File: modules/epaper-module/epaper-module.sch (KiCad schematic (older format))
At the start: 24 parts, among them J1 Conn_01x04, J2 Conn_01x04, Q1 Si1308EDL, U1 WSH-12561

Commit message: EPaper module: add voltage regulator and level switch
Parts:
- added C1: 10uF, Capacitor_SMD:C_0805_2012Metric_Pad1.18x1.45mm_HandSolder, symbol Device:C
- added C13, C14: 100nF, Capacitor_SMD:C_0805_2012Metric_Pad1.18x1.45mm_HandSolder, symbol Device:C
- added C8: 4.7uF, Capacitor_SMD:C_0805_2012Metric_Pad1.18x1.45mm_HandSolder, symbol Device:C
- added U2: MIC5504-3.3YM5, Package_TO_SOT_SMD:SOT-23-5, symbol Regulator_Linear:MIC5504-3.3YM5
- added U3: TXS0108EPW, Package_SO:TSSOP-20_4.4x6.5mm_P0.65mm, symbol Logic_LevelTranslator:TXS0108EPW
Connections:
- net labels added: BUSY', CLK', CS', DC', DIN', RES', VCC
- wire segments 97 -> 135

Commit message: EPaper module: split display into display itself and connector
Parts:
- added DS1: WSH-12561, project_components:WSH-12561, symbol project_components:WSH-12561
- added JP1: Jumper_NC_Dual, Jumper:SolderJumper-3_P2.0mm_Open_TrianglePad1.0x1.5mm, symbol Device:Jumper_NC_Dual
- D1, D2, D3: VendorLink (none) -> https://pl.mouser.com/ProductDetail/onsemi/MBR0530T3G?qs=3J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
- H1, H2, H3, H4: VendorLink (none) -> N/A
- L1: value 10H -> 10uH; footprint Inductor_SMD:L_0805_2012Metric_Pad1.15x1.40mm_HandSolder -> Inductor_SMD:L_TDK_NLV25_2.5x2.0mm; VendorLink (none) -> https://pl.mouser.com/ProductDetail/739-TYA252012100M-10
- Q1: VendorLink (none) -> https://pl.mouser.com/ProductDetail/78-SI1308EDL-T1-BE3
- U2: VendorLink (none) -> https://pl.mouser.com/ProductDetail/Microchip-Technology-Mi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
- U3: VendorLink (none) -> https://pl.mouser.com/ProductDetail/771-NTS0308EPWJ
- XDS1: renamed from U1; value WSH-12561 -> WSH-12561-FFC-MP; footprint epaper-module:WSH-12561 -> Connector_FFC-FPC:TE_2-1734839-4_1x24-1MP_P0.5mm_Horizontal; symbol project_components:WSH-12561 -> project_components:WSH-12561-FFC-MP
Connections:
- net labels added: BS
- wire segments 135 -> 136
- no-connect marks 3 -> 7
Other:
- moved on the sheet: C1, C13, C14, C8, U2, U3

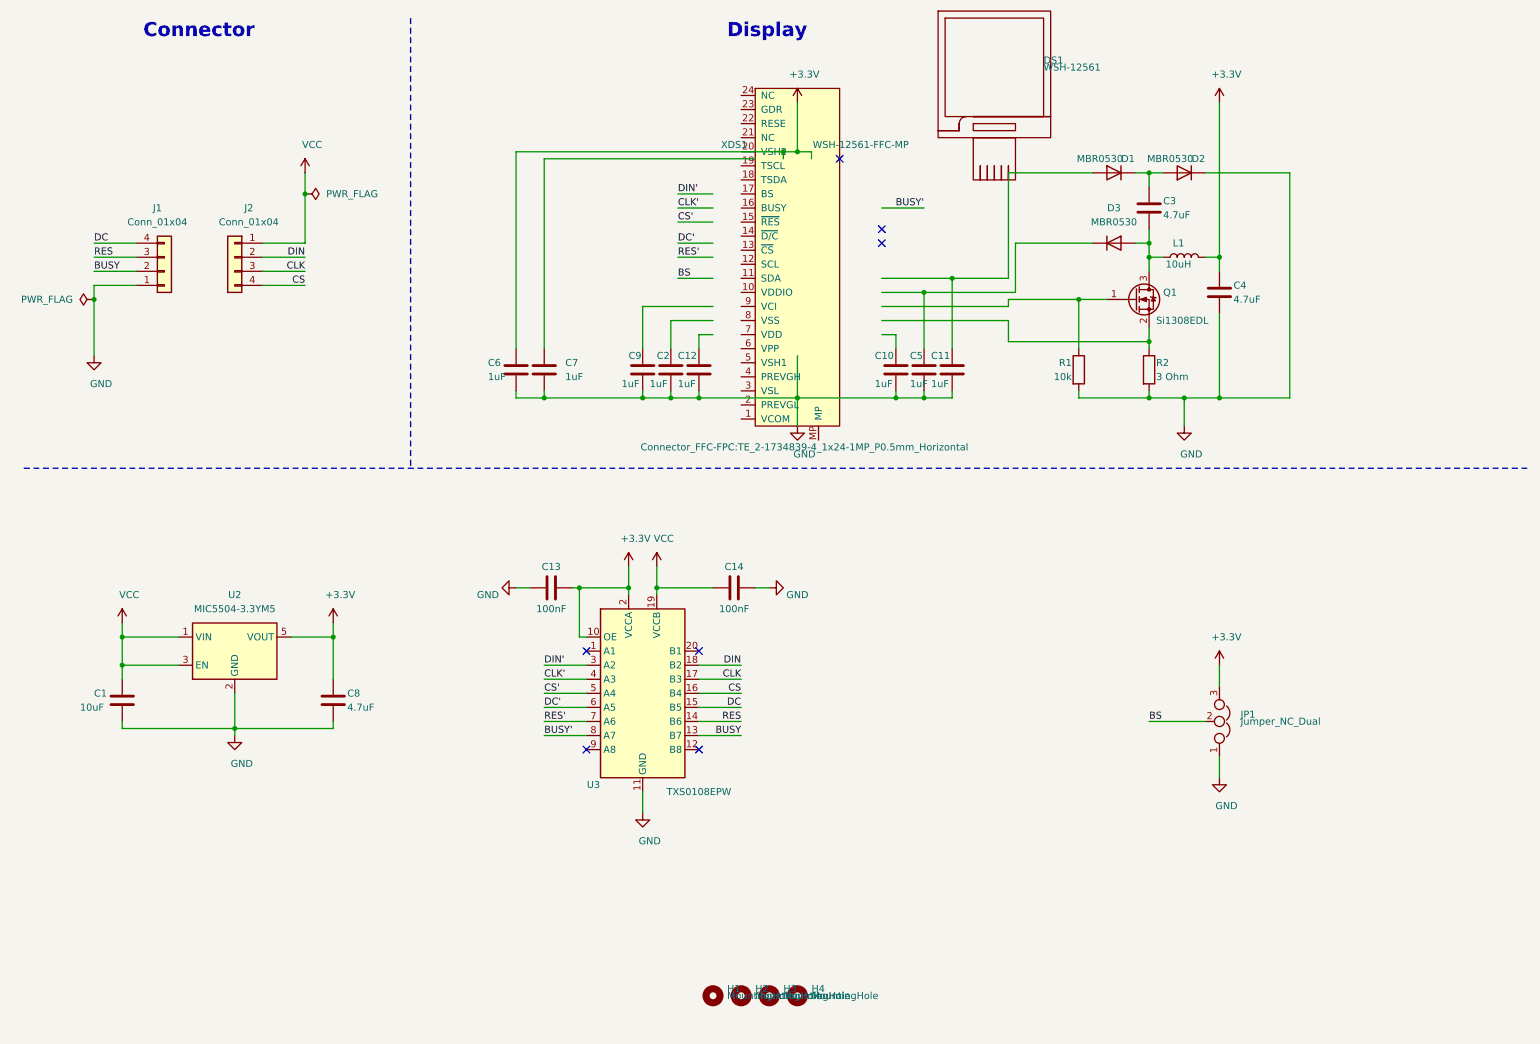
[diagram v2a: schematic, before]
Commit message: EPaper module: reorganize schematic
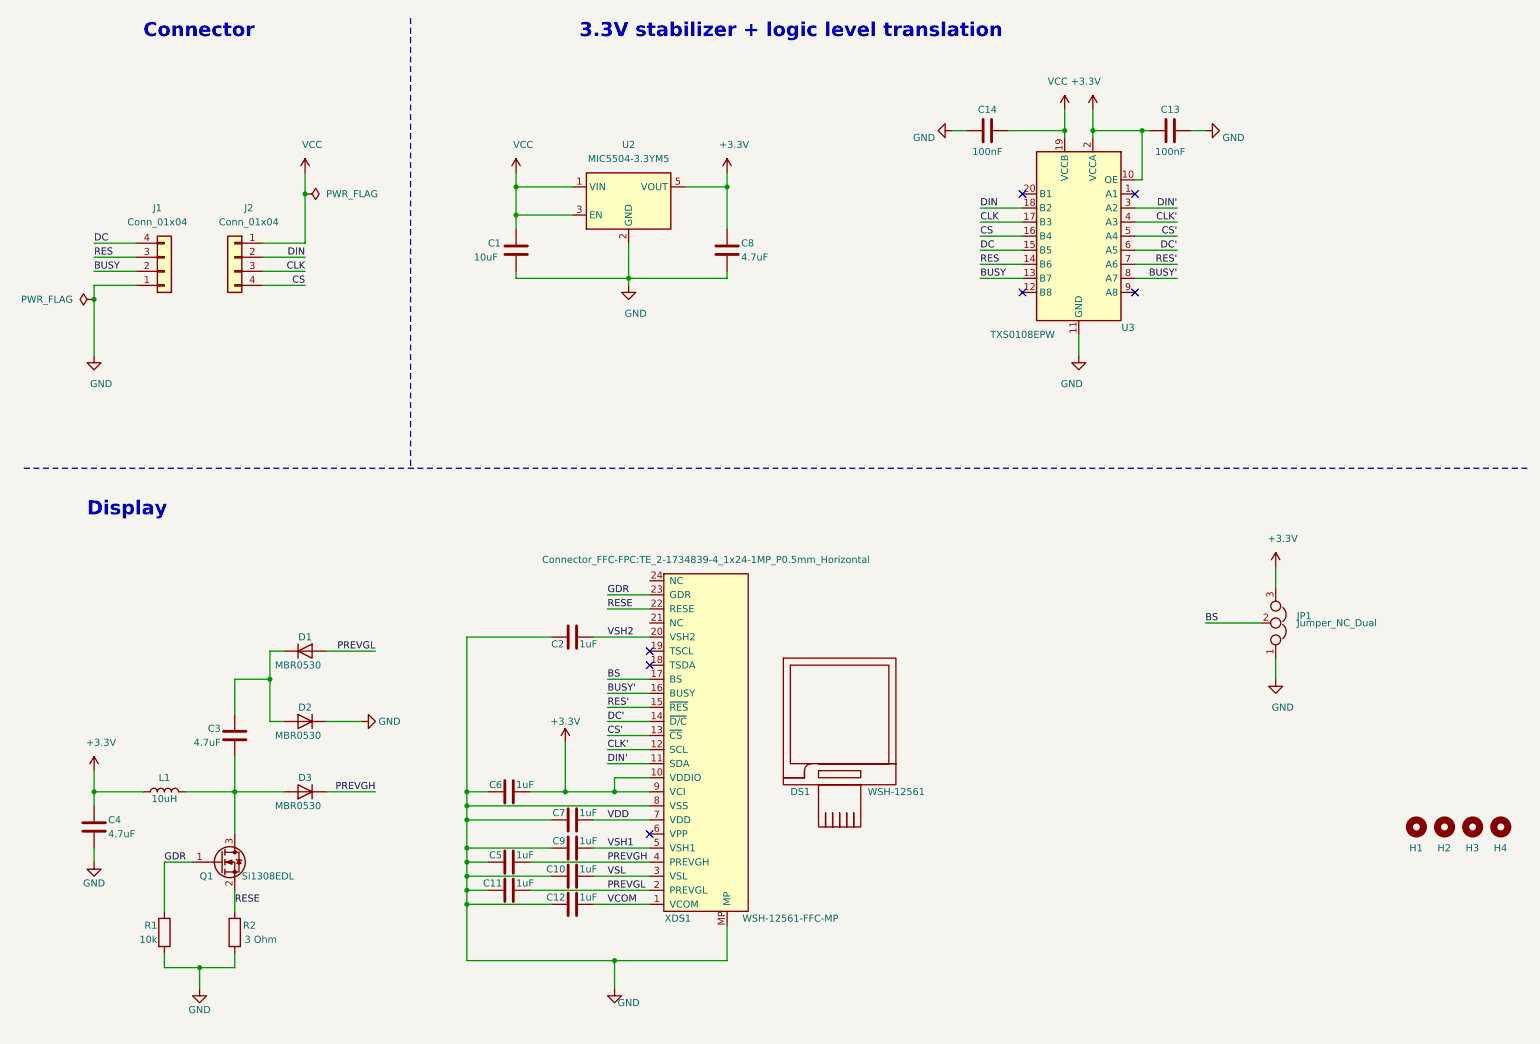
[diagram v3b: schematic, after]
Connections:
- net labels added: GDR, PREVGH, PREVGL, RESE, VCOM, VDD, VSH1, VSH2, VSL
- wire segments 136 -> 122
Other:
- note added: "3.3V stabilizer + logic level translation"
- moved on the sheet: C1, C10, C11, C12, C13, C14, C2, C3, C4, C5, C6, C7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

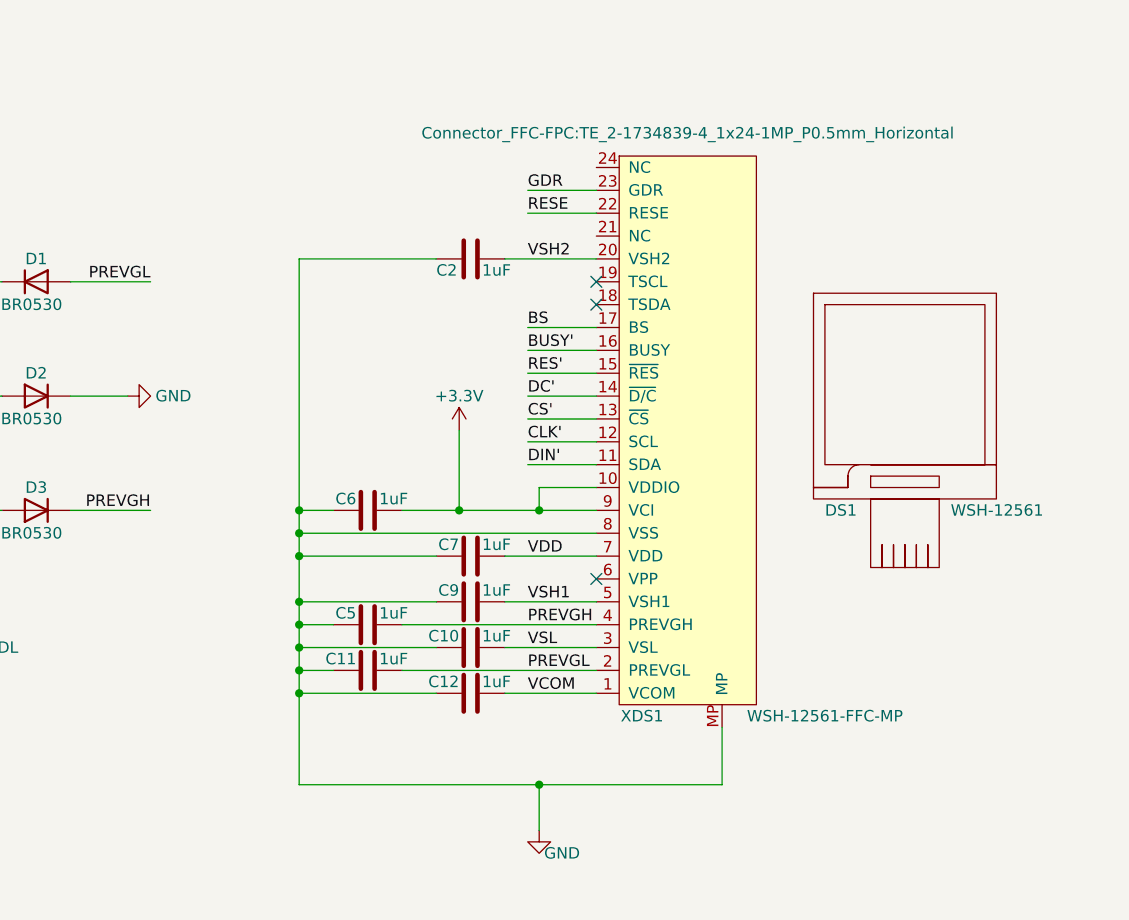
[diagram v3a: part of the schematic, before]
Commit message: EPaper module: add two capacitors from Waveshare module schematic
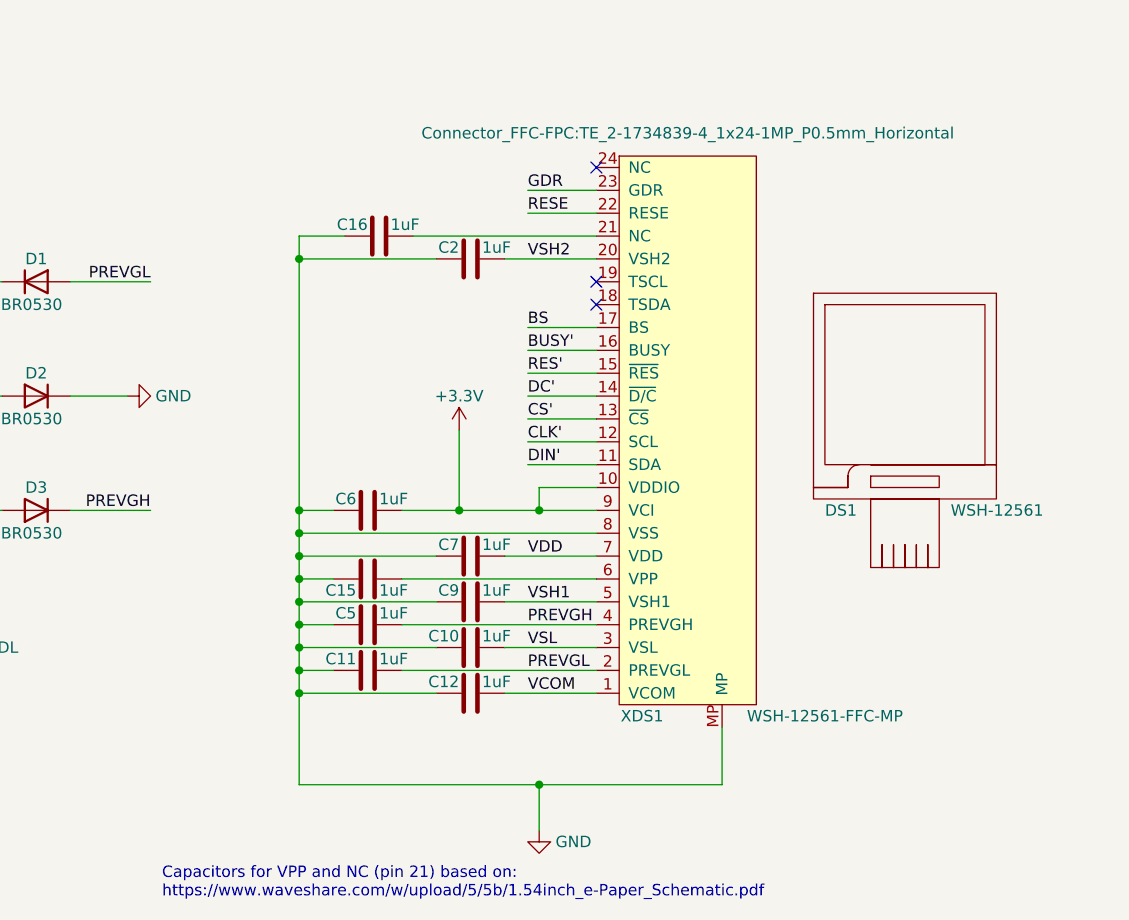
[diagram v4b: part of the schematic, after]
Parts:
- added C15, C16: 1uF, Capacitor_SMD:C_0805_2012Metric_Pad1.18x1.45mm_HandSolder, symbol Device:C
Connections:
- net GND: now also C15.2, C16.2
- net at XDS1.21 (NC): now also C16.1
- net at XDS1.6 (VPP): now also C15.1
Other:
- note added: "Capacitors for VPP and NC (pin 21) based on:\nhttps://www.waveshare.com/w/upload/5/5b/1.54inch_e-Paper_Schematic.pdf"
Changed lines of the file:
@@
 U 1 1 608E029A
 P 4400 4900
-F 0 "C2" V 4350 4750 50  0000 L CNN
-F 1 "1uF" V 4350 4950 50  0000 L CNN
+F 0 "C2" V 4450 4850 50  0000 R CNN
+F 1 "1uF" V 4450 4950 50  0000 L CNN
 F 2 "Capacitor_SMD:C_0805_2012Metric_Pad1.18x1.45mm_HandSolder" H 4438 4750 50  0001 C CNN
 F 3 "~" H 4400 4900 50  0001 C CNN
@@
 P 4700 7400
 F 0 "#PWR0104" H 4700 7150 50  0001 C CNN
-F 1 "GND" H 4800 7300 50  0000 C CNN
+F 1 "GND" H 4850 7350 50  0000 C CNN
 F 2 "" H 4700 7400 50  0001 C CNN
 F 3 "" H 4700 7400 50  0001 C CNN
@@
 $EndComp
 NoConn ~ 4950 5000
-NoConn ~ 4950 6300
 Wire Wire Line
 	4950 5300 4650 5300
@@
 Connection ~ 3650 6200
 Wire Wire Line
-	3650 6200 3650 6400
+	3650 6200 3650 6300
 Wire Wire Line
 	4250 6800 3650 6800
@@
 Text Label 4650 6800 0    50   ~ 0
 VCOM
+NoConn ~ 4950 4500
+$Comp
+L Device:C C16
+U 1 1 61AA5909
+P 4000 4800
+F 0 "C16" V 4050 4750 50  0000 R CNN
+F 1 "1uF" V 4050 4850 50  0000 L CNN
+F 2 "Capacitor_SMD:C_0805_2012Metric_Pad1.18x1.45mm_HandSolder" H 4038 4650 50  0001 C CNN
+F 3 "~" H 4000 4800 50  0001 C CNN
+	1    4000 4800
+	0    1    -1   0
+$EndComp
+Wire Wire Line
+	4150 4800 4950 4800
+Wire Wire Line
+	3850 4800 3650 4800
+Wire Wire Line
+	3650 4800 3650 4900
+Connection ~ 3650 4900
+$Comp
+L Device:C C15
+U 1 1 61AB06F0
+P 3950 6300
+F 0 "C15" V 3900 6250 50  0000 R CNN
+F 1 "1uF" V 3900 6350 50  0000 L CNN
+F 2 "Capacitor_SMD:C_0805_2012Metric_Pad1.18x1.45mm_HandSolder" H 3988 6150 50  0001 C CNN
+F 3 "~" H 3950 6300 50  0001 C CNN
+	1    3950 6300
+	0    1    -1   0
+$EndComp
+Wire Wire Line
+	3650 6300 3800 6300
+Connection ~ 3650 6300
+Wire Wire Line
+	3650 6300 3650 6400
+Wire Wire Line
+	4100 6300 4950 6300
+Text Notes 3050 7700 0    50   ~ 0
+Capacitors for VPP and NC (pin 21) based on:\nhttps://www.waveshare.com/w/upload/5/5b/1.54inch_e-Paper_Schematic.pdf
 $EndSCHEMATC

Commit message: EPaper module: reannotate schematic
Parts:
- renumbered C16 to C1, C12 to C10, C4 to C11, C3 to C12, C1 to C13, C8 to C14, C14 to C15, C13 to C16, C6 to C3, C7 to C4, C15 to C5, C9 to C6, C5 to C7, C10 to C8, C11 to C9, U2 to U1, U3 to U2
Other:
- moved on the sheet: C1, C13, C14, C15, C16, U1, U2
